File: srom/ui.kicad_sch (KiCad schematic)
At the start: 5 parts, among them J301 Conn_01x05_Female, J302 Conn_01x04_Female, J303 Conn_01x03_Female, U301 Pico-3 UI

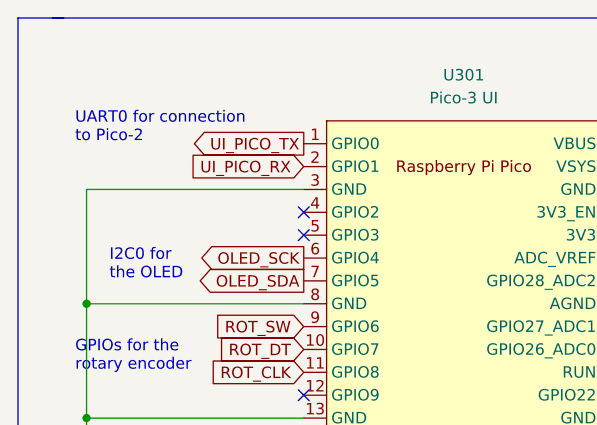
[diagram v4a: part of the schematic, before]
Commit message: move the ZXWAIT signal on pico2 off the SP1 connection. matches latest hardware
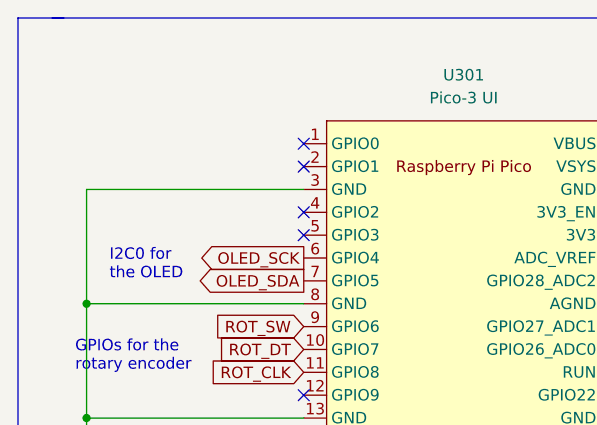
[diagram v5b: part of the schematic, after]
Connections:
- net UI_PICO_RX: no longer names the net of U301.2 (GPIO1)
- net UI_PICO_TX: no longer names the net of U301.1 (GPIO0)
- no-connect marks 18 -> 20
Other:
- note removed: "UART0 for connection to Pico-2"
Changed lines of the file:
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@@
   (junction (at 30.48 66.04) (diameter 0) (color 0 0 0 0)
   )
+  (no_connect (at 54.61 35.56))
   (no_connect (at 54.61 71.12))
   (no_connect (at 54.61 45.72))
   (no_connect (at 54.61 81.28))
+  (no_connect (at 54.61 38.1))
   (no_connect (at 54.61 63.5))
   (no_connect (at 90.17 55.88))
@@
     (effects (font (size 1.27 1.27)) (justify left bottom))
   )
-  (text "UART0 for connection\nto Pico-2" (at 29.21 35.56 0)
-    (effects (font (size 1.27 1.27)) (justify left bottom))
-  )
   (text "Currently assuming a rotary encoder as input device"
     (at 134.62 129.54 0)
@@
     )
   )
-  (global_label "UI_PICO_TX" (shape output) (at 54.61 35.56 180) (fields_autoplaced)
-    (effects (font (size 1.27 1.27)) (justify right))
-    (property "Intersheet References" "${INTERSHEET_REFS}" (id 0) (at 41.674 35.4806 0)
-      (effects (font (size 1.27 1.27)) (justify right) hide)
-    )
-  )
   (global_label "OLED_SDA" (shape output) (at 243.84 119.38 0) (fields_autoplaced)
     (effects (font (size 1.27 1.27)) (justify left))
@@
       (effects (font (size 1.27 1.27)) (justify right) hide)
     )
-  )
-  (global_label "UI_PICO_RX" (shape input) (at 54.61 38.1 180) (fields_autoplaced)
-    (effects (font (size 1.27 1.27)) (justify right))
-    (property "Intersheet References" "${INTERSHEET_REFS}" (id 0) (at 41.3717 38.0206 0)
-      (effects (font (size 1.27 1.27)) (justify right) hide)
-    )

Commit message: start updating schematic for next board
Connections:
- net SPI1_UI_MISO: now reaches U301.16 (GPIO12)
- net SPI1_UI_SLAVE_ENABLE: now reaches U301.17 (GPIO13)
- net SPI1_UI_CLK: now reaches U301.19 (GPIO14)
- net SPI1_UI_MOSI: now reaches U301.20 (GPIO15)
- no-connect marks 20 -> 16
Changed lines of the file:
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@@
   (title_block
     (title "Pico Interface One")
-    (date "2023-04-13")
-    (rev "v1.2 to v1.3 WIP")
+    (date "2023-04-15")
+    (rev "v1.3")
   )
   (junction (at 99.06 38.1) (diameter 0) (color 0 0 0 0)
@@
   (no_connect (at 54.61 71.12))
   (no_connect (at 54.61 45.72))
-  (no_connect (at 54.61 81.28))
   (no_connect (at 54.61 38.1))
   (no_connect (at 54.61 63.5))
@@
   (no_connect (at 54.61 68.58))
   (no_connect (at 90.17 43.18))
-  (no_connect (at 54.61 76.2))
   (no_connect (at 90.17 60.96))
   (no_connect (at 54.61 43.18))
-  (no_connect (at 54.61 83.82))
   (no_connect (at 90.17 35.56))
   (no_connect (at 90.17 58.42))
-  (no_connect (at 54.61 73.66))
   (no_connect (at 90.17 63.5))
   (no_connect (at 202.565 60.96))
@@
     )
   )
+  (global_label "SPI1_UI_CLK" (shape output) (at 54.61 81.28 180) (fields_autoplaced)
+    (effects (font (size 1.27 1.27)) (justify right))
+    (property "Intersheet References" "${INTERSHEET_REFS}" (id 0) (at 40.4645 81.2006 0)
+      (effects (font (size 1.27 1.27)) (justify right) hide)
+    )
+  )
   (global_label "MOSI_DI" (shape input) (at 207.01 41.91 0) (fields_autoplaced)
     (effects (font (size 1.27 1.27)) (justify left))
@@
     )
   )
+  (global_label "SPI1_UI_MOSI" (shape output) (at 54.61 83.82 180) (fields_autoplaced)
+    (effects (font (size 1.27 1.27)) (justify right))
+    (property "Intersheet References" "${INTERSHEET_REFS}" (id 0) (at 39.4364 83.7406 0)
+      (effects (font (size 1.27 1.27)) (justify right) hide)
+    )
+  )
   (global_label "3V3_PICO3" (shape input) (at 165.1 115.57 0) (fields_autoplaced)
     (effects (font (size 1.27 1.27)) (justify left))
@@
     )
   )
+  (global_label "SPI1_UI_SLAVE_ENABLE" (shape output) (at 54.61 76.2 180) (fields_autoplaced)
+    (effects (font (size 1.27 1.27)) (justify right))
+    (property "Intersheet References" "${INTERSHEET_REFS}" (id 0) (at 30.4859 76.1206 0)
+      (effects (font (size 1.27 1.27)) (justify right) hide)
+    )
+  )
   (global_label "3V3_PICO3" (shape input) (at 245.11 114.3 0) (fields_autoplaced)
     (effects (font (size 1.27 1.27)) (justify left))
@@
       (effects (font (size 1.27 1.27)) (justify right) hide)
     )
+  )
+  (global_label "SPI1_UI_MISO" (shape input) (at 54.61 73.66 180) (fields_autoplaced)
+    (effects (font (size 1.27 1.27)) (justify right))
+    (property "Intersheet References" "${INTERSHEET_REFS}" (id 0) (at 39.4364 73.5806 0)
+      (effects (font (size 1.27 1.27)) (justify right) hide)
+    )

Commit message: first draft of layout of board 2
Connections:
- net MISO_D0 renamed SPI0_SD_MISO
- net MOSI_DI renamed SPI0_SD_MOSI
- net SD_CLK renamed SPI0_SD_CLK
- net SD_DAT1: no longer names the net of XS301.8 (DAT1)
- net SD_DAT1: no longer U301.26 (GPIO20)
- net SD_DAT2: no longer names the net of XS301.1 (DAT2)
- net SD_DAT2: no longer U301.27 (GPIO21)
- net SD_SS renamed SPI0_SD_SLAVE_ENABLE
- no-connect marks 16 -> 20
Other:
- note added: "SPI0 Master, to IO Pico"
- note added: "SPI1 Master, to SD card"
- note removed: "Assume SPI0 for the SD card. Connect SDBus as well, just in case"
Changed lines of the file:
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@@
   (junction (at 30.48 66.04) (diameter 0) (color 0 0 0 0)
   )
+  (no_connect (at 207.01 49.53))
   (no_connect (at 54.61 35.56))
   (no_connect (at 54.61 71.12))
@@
   (no_connect (at 54.61 68.58))
   (no_connect (at 90.17 43.18))
+  (no_connect (at 90.17 68.58))
   (no_connect (at 90.17 60.96))
   (no_connect (at 54.61 43.18))
+  (no_connect (at 90.17 71.12))
+  (no_connect (at 207.01 53.34))
   (no_connect (at 90.17 35.56))
   (no_connect (at 90.17 58.42))
@@
     (effects (font (size 1.27 1.27)) (justify left bottom))
   )
+  (text "SPI1 Master,\nto SD card" (at 94.996 93.98 0)
+    (effects (font (size 1.27 1.27)) (justify left bottom))
+  )
   (text "Currently assuming a rotary encoder as input device"
     (at 134.62 129.54 0)
@@
     (effects (font (size 1.27 1.27)) (justify left bottom))
   )
-  (text "Assume SPI0 for the\nSD card. Connect SDBus\nas well, just in case"
-    (at 102.87 74.93 0)
-    (effects (font (size 1.27 1.27)) (justify left bottom))
-  )
   (text "GPIOs for the\nrotary encoder" (at 29.21 60.96 0)
+    (effects (font (size 1.27 1.27)) (justify left bottom))
+  )
+  (text "SPI0 Master,\nto IO Pico" (at 38.608 94.234 0)
     (effects (font (size 1.27 1.27)) (justify left bottom))
   )
@@
     )
   )
-  (global_label "MOSI_DI" (shape input) (at 207.01 41.91 0) (fields_autoplaced)
-    (effects (font (size 1.27 1.27)) (justify left))
-    (property "Intersheet References" "${INTERSHEET_REFS}" (id 0) (at 168.275 -65.405 0)
-      (effects (font (size 1.27 1.27)) hide)
+  (global_label "SPI0_SD_MOSI" (shape input) (at 207.01 41.91 0) (fields_autoplaced)
+    (effects (font (size 1.27 1.27)) (justify left))
+    (property "Intersheet References" "${INTERSHEET_REFS}" (id 0) (at 222.7279 41.8306 0)
+      (effects (font (size 1.27 1.27)) (justify left) hide)
     )
   )
@@
     )
   )
-  (global_label "SD_DAT1" (shape input) (at 207.01 53.34 0) (fields_autoplaced)
-    (effects (font (size 1.27 1.27)) (justify left))
-    (property "Intersheet References" "${INTERSHEET_REFS}" (id 0) (at 168.275 -65.405 0)
-      (effects (font (size 1.27 1.27)) hide)
-    )
-  )
   (global_label "ROT_CLK" (shape output) (at 148.59 123.19 0) (fields_autoplaced)
     (effects (font (size 1.27 1.27)) (justify left))
@@
     )
   )
-  (global_label "SD_CLK" (shape input) (at 90.17 76.2 0) (fields_autoplaced)
-    (effects (font (size 1.27 1.27)) (justify left))
-    (property "Intersheet References" "${INTERSHEET_REFS}" (id 0) (at 20.955 13.97 0)
-      (effects (font (size 1.27 1.27)) hide)
-    )
-  )
   (global_label "OLED_SDA" (shape output) (at 243.84 119.38 0) (fields_autoplaced)
     (effects (font (size 1.27 1.27)) (justify left))
@@
     )
   )
-  (global_label "SD_DAT1" (shape input) (at 90.17 71.12 0) (fields_autoplaced)
-    (effects (font (size 1.27 1.27)) (justify left))
-    (property "Intersheet References" "${INTERSHEET_REFS}" (id 0) (at 20.955 13.97 0)
-      (effects (font (size 1.27 1.27)) hide)
-    )
-  )
   (global_label "SPI1_UI_SLAVE_ENABLE" (shape output) (at 54.61 76.2 180) (fields_autoplaced)
     (effects (font (size 1.27 1.27)) (justify right))
@@
     )
   )
-  (global_label "SD_DAT2" (shape input) (at 90.17 68.58 0) (fields_autoplaced)
-    (effects (font (size 1.27 1.27)) (justify left))
-    (property "Intersheet References" "${INTERSHEET_REFS}" (id 0) (at 20.955 13.97 0)
-      (effects (font (size 1.27 1.27)) hide)
-    )
-  )
   (global_label "SWDCLK_P3" (shape input) (at 43.815 153.035 0) (fields_autoplaced)
     (effects (font (size 1.27 1.27)) (justify left))
@@
     )
   )
-  (global_label "SD_DAT2" (shape input) (at 207.01 49.53 0) (fields_autoplaced)
-    (effects (font (size 1.27 1.27)) (justify left))
-    (property "Intersheet References" "${INTERSHEET_REFS}" (id 0) (at 168.275 -65.405 0)
-      (effects (font (size 1.27 1.27)) hide)
-    )
-  )
   (global_label "ROT_DT" (shape input) (at 54.61 58.42 180) (fields_autoplaced)
     (effects (font (size 1.27 1.27)) (justify right))
@@
     )
   )
-  (global_label "MOSI_DI" (shape input) (at 90.17 73.66 0) (fields_autoplaced)
-    (effects (font (size 1.27 1.27)) (justify left))
-    (property "Intersheet References" "${INTERSHEET_REFS}" (id 0) (at 20.955 13.97 0)
-      (effects (font (size 1.27 1.27)) hide)
+  (global_label "SPI0_SD_SLAVE_ENABLE" (shape output) (at 90.17 81.28 0) (fields_autoplaced)
+    (effects (font (size 1.27 1.27)) (justify left))
+    (property "Intersheet References" "${INTERSHEET_REFS}" (id 0) (at 114.8383 81.2006 0)
+      (effects (font (size 1.27 1.27)) (justify left) hide)
+    )
+  )
+  (global_label "SPI0_SD_MOSI" (shape output) (at 90.17 73.66 0) (fields_autoplaced)
+    (effects (font (size 1.27 1.27)) (justify left))
+    (property "Intersheet References" "${INTERSHEET_REFS}" (id 0) (at 105.8879 73.5806 0)
+      (effects (font (size 1.27 1.27)) (justify left) hide)
     )
   )
@@
     )
   )
-  (global_label "SD_CLK" (shape input) (at 207.01 38.1 0) (fields_autoplaced)
-    (effects (font (size 1.27 1.27)) (justify left))
-    (property "Intersheet References" "${INTERSHEET_REFS}" (id 0) (at 168.275 -65.405 0)
-      (effects (font (size 1.27 1.27)) hide)
-    )
-  )
-  (global_label "SD_SS" (shape input) (at 90.17 81.28 0) (fields_autoplaced)
-    (effects (font (size 1.27 1.27)) (justify left))
-    (property "Intersheet References" "${INTERSHEET_REFS}" (id 0) (at 20.955 31.75 0)
-      (effects (font (size 1.27 1.27)) hide)
+  (global_label "SPI0_SD_CLK" (shape input) (at 207.01 38.1 0) (fields_autoplaced)
+    (effects (font (size 1.27 1.27)) (justify left))
+    (property "Intersheet References" "${INTERSHEET_REFS}" (id 0) (at 221.6998 38.0206 0)
+      (effects (font (size 1.27 1.27)) (justify left) hide)
+    )
+  )
+  (global_label "SPI0_SD_CLK" (shape output) (at 90.17 76.2 0) (fields_autoplaced)
+    (effects (font (size 1.27 1.27)) (justify left))
+    (property "Intersheet References" "${INTERSHEET_REFS}" (id 0) (at 104.8598 76.1206 0)
+      (effects (font (size 1.27 1.27)) (justify left) hide)
     )
   )
@@
     )
   )
-  (global_label "SD_SS" (shape input) (at 207.01 45.72 0) (fields_autoplaced)
-    (effects (font (size 1.27 1.27)) (justify left))
-    (property "Intersheet References" "${INTERSHEET_REFS}" (id 0) (at 168.275 -65.405 0)
-      (effects (font (size 1.27 1.27)) hide)
-    )
-  )
-  (global_label "MISO_D0" (shape input) (at 207.01 57.15 0) (fields_autoplaced)
-    (effects (font (size 1.27 1.27)) (justify left))
-    (property "Intersheet References" "${INTERSHEET_REFS}" (id 0) (at 168.275 -65.405 0)
-      (effects (font (size 1.27 1.27)) hide)
-    )
-  )
-  (global_label "MISO_D0" (shape input) (at 90.17 83.82 0) (fields_autoplaced)
-    (effects (font (size 1.27 1.27)) (justify left))
-    (property "Intersheet References" "${INTERSHEET_REFS}" (id 0) (at 20.955 13.97 0)
-      (effects (font (size 1.27 1.27)) hide)
-    )
-  )
+  (global_label "SPI0_SD_SLAVE_ENABLE" (shape input) (at 207.01 45.72 0) (fields_autoplaced)
+    (effects (font (size 1.27 1.27)) (justify left))
+    (property "Intersheet References" "${INTERSHEET_REFS}" (id 0) (at 231.6783 45.6406 0)
+      (effects (font (size 1.27 1.27)) (justify left) hide)
+    )
+  )
+  (global_label "SPI0_SD_MISO" (shape output) (at 207.01 57.15 0) (fields_autoplaced)
+    (effects (font (size 1.27 1.27)) (justify left))
+    (property "Intersheet References" "${INTERSHEET_REFS}" (id 0) (at 222.7279 57.0706 0)
+      (effects (font (size 1.27 1.27)) (justify left) hide)
+    )
+  )
+  (global_label "SPI0_SD_MISO" (shape input) (at 90.17 83.82 0) (fields_autoplaced)
+    (effects (font (size 1.27 1.27)) (justify left))
+    (property "Intersheet References" "${INTERSHEET_REFS}" (id 0) (at 105.8879 83.7406 0)
+      (effects (font (size 1.27 1.27)) (justify left) hide)
+    )
+  )

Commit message: v1.3 of the board off to production
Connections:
- net TEST_BLIPPER_P3: now reaches U301.14 (GPIO10)
- no-connect marks 20 -> 19
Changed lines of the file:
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@@
   (no_connect (at 90.17 55.88))
   (no_connect (at 90.17 48.26))
-  (no_connect (at 54.61 68.58))
   (no_connect (at 90.17 43.18))
   (no_connect (at 90.17 68.58))
@@
       (effects (font (size 1.27 1.27)) (justify right) hide)
     )
+  )
+  (global_label "TEST_BLIPPER_P3" (shape output) (at 54.61 68.58 180) (fields_autoplaced)
+    (effects (font (size 1.27 1.27)) (justify right))
+    (property "Intersheet References" "${INTERSHEET_REFS}" (id 0) (at 35.6264 68.5006 0)
+      (effects (font (size 1.27 1.27)) (justify right) hide)
+    )
